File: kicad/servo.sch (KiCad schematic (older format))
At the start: 0 parts

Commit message: Come back to moldova to finish schematics and begin layout
I've started again from Moldova to discuss with Alexander the details.
I'm now working with schematics requeriments.
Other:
- note added: "TEMP"
- note added: "UI"
- note added: "uC\nADC"
- note added: "uC\nCLK\nDbg"
- note added: "uC\nGPIO"
- note removed: "ADC"
- note removed: "CLK\nDBG"
- note removed: "GPIO"
- note removed: "SHUNT\n SD"
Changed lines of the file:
@@
 $Descr A3 16535 11693
 encoding utf-8
-Sheet 1 16
+Sheet 1 17
 Title "servo drive"
 Date "25 10 2019"
@@
 $EndSheet
 $Sheet
-S 7500 7450 1300 1150
+S 5750 7450 1300 1150
 U 5DD0E9D6
-F0 "adc" 50
-F1 "adc.sch" 50
+F0 "uc_adc" 50
+F1 "uc_adc.sch" 50
 $EndSheet
 $Sheet
@@
 $EndSheet
 $Sheet
-S 7500 5900 1300 1150
+S 5750 5900 1300 1150
 U 5EAA846A
-F0 "power" 50
-F1 "power.sch" 50
+F0 "uc_power" 50
+F1 "uc_power.sch" 50
 $EndSheet
 $Sheet
-S 7500 4400 1300 1150
+S 5750 4400 1300 1150
 U 5DD4DF4C
-F0 "clk" 50
-F1 "clk.sch" 50
+F0 "uc_clk_dbg" 50
+F1 "uc_clk_dbg.sch" 50
 $EndSheet
 $Sheet
-S 4100 5900 1300 1150
+S 2350 5900 1300 1150
 U 5DD76B18
 F0 "ac_in" 50
@@
 $EndSheet
 $Sheet
-S 5750 5900 1300 1150
+S 4000 5900 1300 1150
 U 5DF5EE96
 F0 "lem" 50
 F1 "lem.sch" 50
 $EndSheet
-Text Notes 6100 6550 0    197  ~ 39
+Text Notes 4350 6550 0    197  ~ 39
 LEM
-Text Notes 7800 8100 0    197  ~ 39
-ADC
+Text Notes 6050 8300 0    197  ~ 39
+uC\nADC
 $Sheet
-S 5750 7450 1300 1150
+S 4000 7450 1300 1150
 U 5DDE8C5E
 F0 "igbt" 50
 F1 "igbt.sch" 50
 $EndSheet
-Text Notes 6100 8100 0    197  ~ 39
+Text Notes 4350 8100 0    197  ~ 39
 IGBT
-Text Notes 7750 6700 0    197  ~ 39
+Text Notes 5950 6750 0    197  ~ 39
 uC \nPower
 Text Notes 9550 8300 0    197  ~ 39
@@
 S 7500 2900 1300 1150
 U 5DE49152
-F0 "gpio" 50
-F1 "gpio.sch" 50
+F0 "temp" 50
+F1 "temp.sch" 50
 $EndSheet
 Text Notes 7750 3600 0    197  ~ 39
-GPIO
-Text Notes 4550 6700 0    197  ~ 39
+TEMP
+Text Notes 2800 6700 0    197  ~ 39
 AC\nIN
 Text Notes 9500 6700 0    197  ~ 39
 Ether\nNET
-Text Notes 7800 5250 0    197  ~ 39
-CLK\nDBG
+Text Notes 6000 5400 0    197  ~ 39
+uC\nCLK\nDbg
 Text Notes 9500 5050 0    197  ~ 39
 ENDAT
@@
 CAN
 $Sheet
-S 5750 4400 1300 1150
-U 5DEE980E
-F0 "shunt sigma delta" 50
-F1 "shunt_sd.sch" 50
-$EndSheet
-Text Notes 5900 5300 0    197  ~ 39
-SHUNT\n  SD
-$Sheet
-S 5750 2900 1300 1150
+S 4000 2900 1300 1150
 U 5E2F3BE3
 F0 "shunt isolated" 50
 F1 "shunt_iso.sch" 50
 $EndSheet
-Text Notes 5900 3800 0    197  ~ 39
+Text Notes 4150 3800 0    197  ~ 39
 SHUNT\n ISO
+$Sheet
+S 5750 2900 1300 1150
+U 5E033FE4
+F0 "uc_gpio" 50
+F1 "uc_gpio.sch" 50
+$EndSheet
+Text Notes 6050 3750 0    197  ~ 39
+uC\nGPIO
+$Sheet
+S 7500 4400 1300 1150
+U 5E0D58C4
+F0 "ui" 50
+F1 "ui.sch" 50
+$EndSheet
+Text Notes 7950 5100 0    197  ~ 39
+UI
 $EndSCHEMATC

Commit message: added isolated gpi, change digital iso gpo from 2 to 8
I've found some Silabs IC's that match better than texas, are cheaper
and on stock. For digital isolation the GPIO to IGBT and data input from
QRP  and GPI from external switches.
I'm adding these IC's and clean the schematics a lots.
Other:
- note added: "ISO\nGPIO\n"
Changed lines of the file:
@@
 $Descr A3 16535 11693
 encoding utf-8
-Sheet 1 17
+Sheet 1 18
 Title "servo drive"
 Date "25 10 2019"
@@
 S 7500 4400 1300 1150
 U 5E0D58C4
+F0 "isolated gpio" 50
+F1 "iso_gipo.sch" 50
+$EndSheet
+Text Notes 7750 5250 0    197  ~ 39
+ISO\nGPIO\n
+$Sheet
+S 7500 5900 1300 1150
+U 5E72D841
 F0 "ui" 50
 F1 "ui.sch" 50
 $EndSheet
-Text Notes 7950 5100 0    197  ~ 39
+Text Notes 7950 6600 0    197  ~ 39
 UI
 $EndSCHEMATC

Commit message: I've decided LEM lxs series, it's the best..
I've decided to use the LEM lxs, is a new series better than LTS and is
pin to pin compatible with the old one and also CAS series, so I think
it's a good option. 0.5usec rise time, multi prymari turns options, and
so..
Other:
- note added: "SHUNT\nSDELTA"
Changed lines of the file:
@@
 $Descr A3 16535 11693
 encoding utf-8
-Sheet 1 18
+Sheet 1 19
 Title "servo drive"
 Date "25 10 2019"
@@
 F1 "ac_in.sch" 50
 $EndSheet
-$Sheet
-S 4000 5900 1300 1150
-U 5DF5EE96
-F0 "lem" 50
-F1 "lem.sch" 50
-$EndSheet
-Text Notes 4350 6550 0    197  ~ 39
-LEM
 Text Notes 6050 8300 0    197  ~ 39
 uC\nADC
@@
 S 4000 2900 1300 1150
 U 5E2F3BE3
-F0 "shunt isolated" 50
-F1 "shunt_iso.sch" 50
+F0 "shunt isigma delta" 50
+F1 "shunt_sd.sch" 50
 $EndSheet
 Text Notes 4150 3800 0    197  ~ 39
-SHUNT\n ISO
+SHUNT\nSDELTA
 $Sheet
 S 5750 2900 1300 1150
@@
 Text Notes 7950 6600 0    197  ~ 39
 UI
+$Sheet
+S 4000 4450 1300 1150
+U 605B70F2
+F0 "lem" 50
+F1 "lem.sch" 50
+$EndSheet
+Text Notes 4300 5200 0    197  ~ 39
+LEM
+$Sheet
+S 4050 5850 1300 1150
+U 605BEC04
+F0 "shunt isolated" 50
+F1 "shunt_iso.sch" 50
+$EndSheet
+Text Notes 4200 6750 0    197  ~ 39
+SHUNT\n ISO
 $EndSCHEMATC

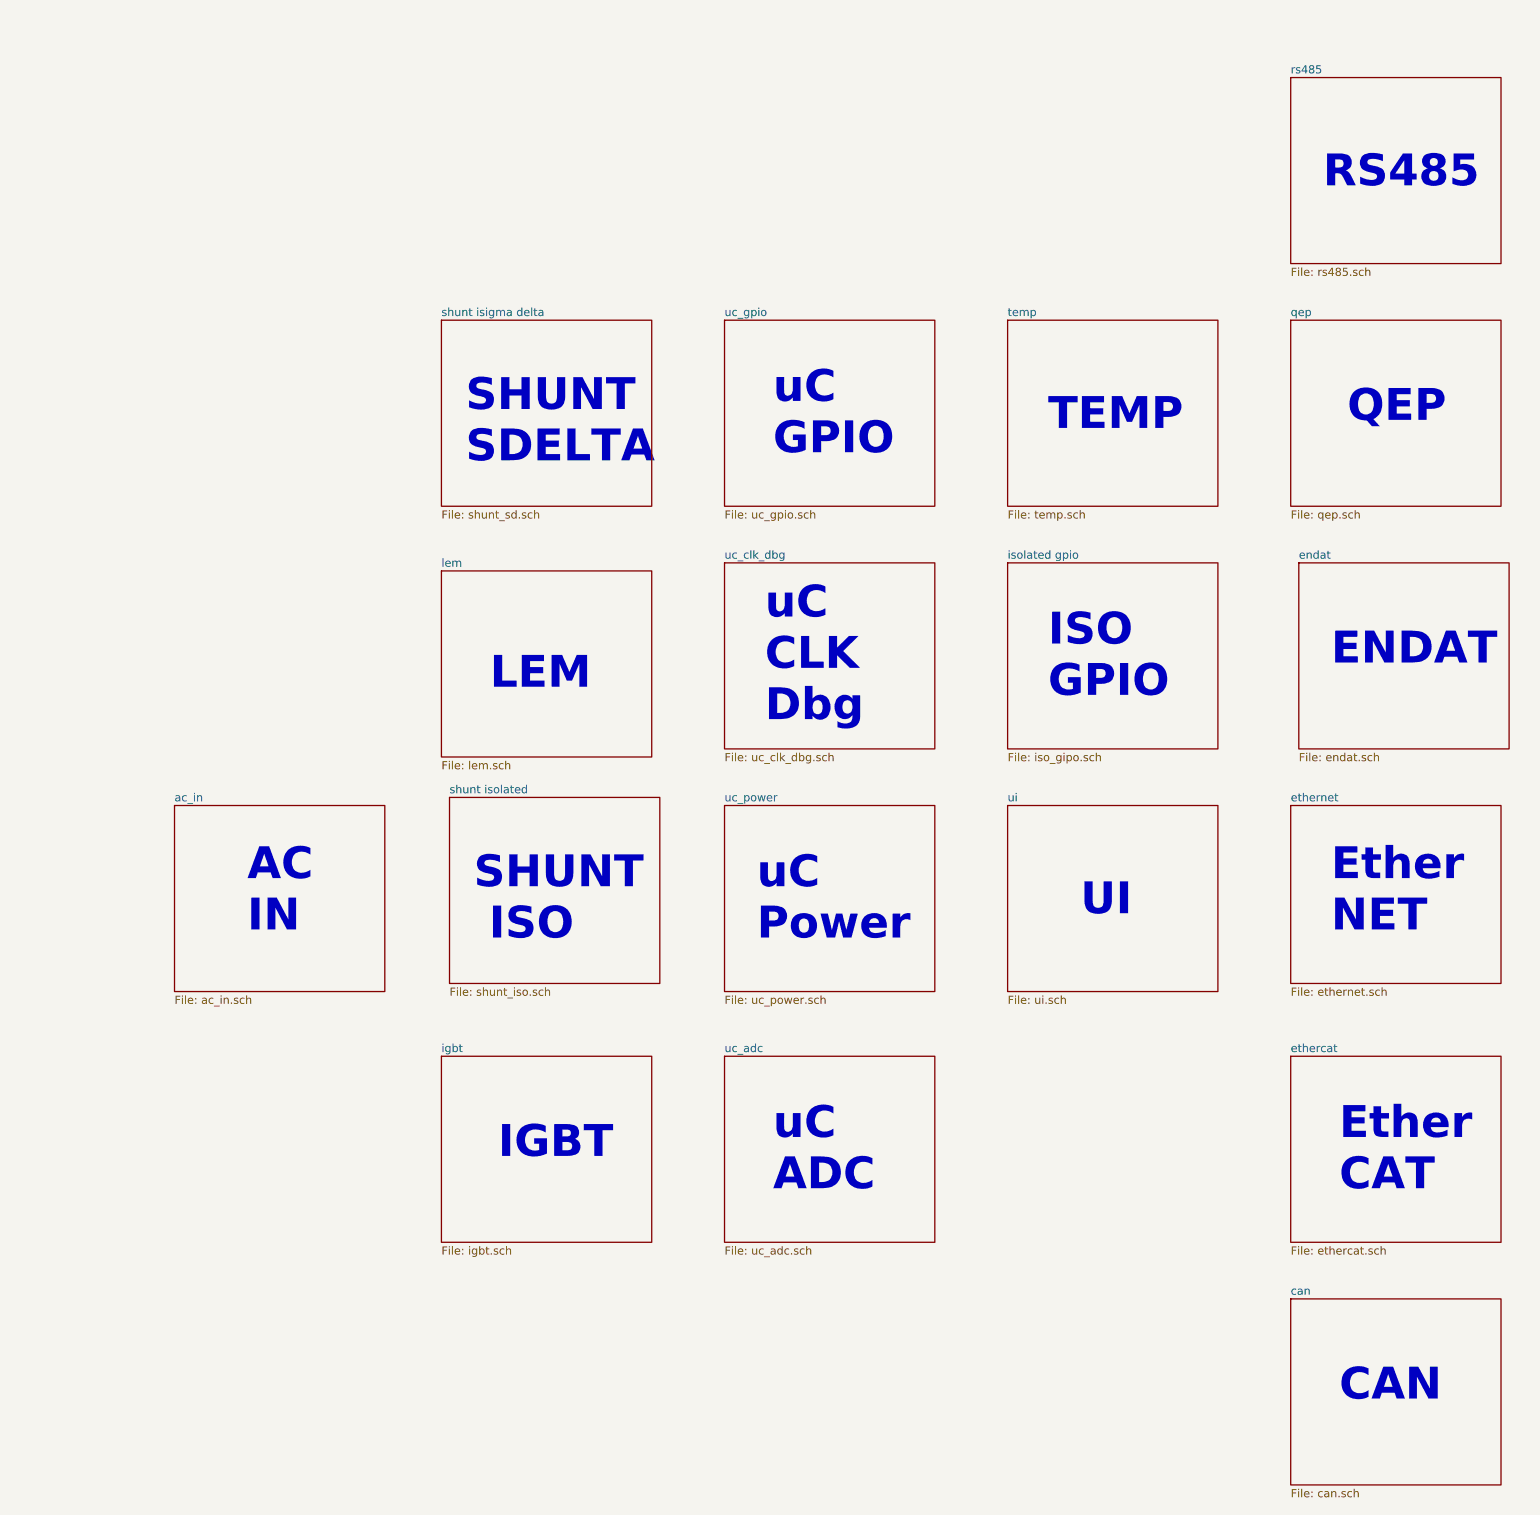
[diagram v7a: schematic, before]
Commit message: I've added LCD UI interfase, EQEP and finish ENDAT
I think I have almos all the interfases ready, I'm begining the
verigication process and then the part definig
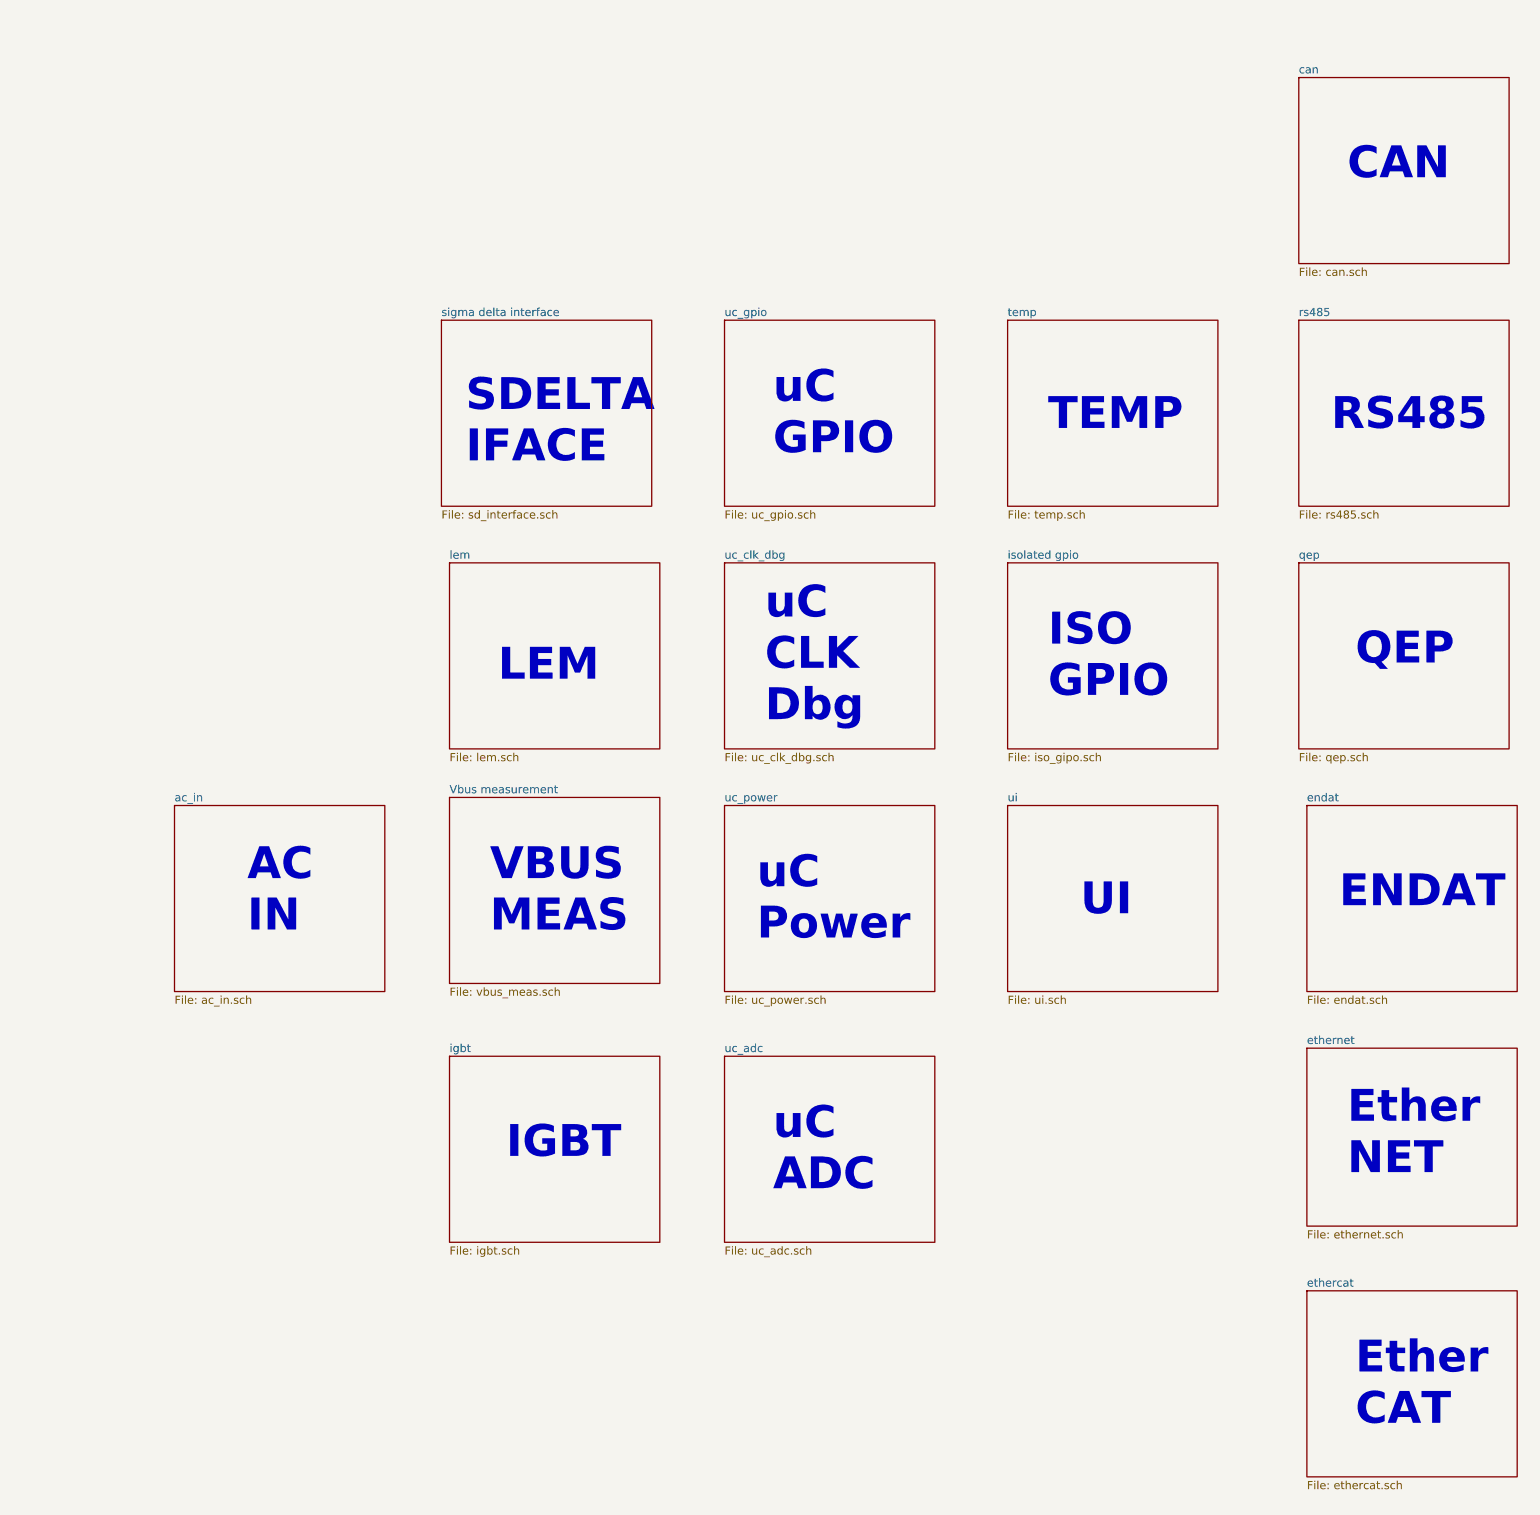
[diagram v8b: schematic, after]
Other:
- note added: "SDELTA\nIFACE"
- note added: "VBUS\nMEAS"
- note removed: "SHUNT\n ISO"
- note removed: "SHUNT\nSDELTA"
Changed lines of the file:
@@
 $EndDescr
 $Sheet
-S 9250 5900 1300 1100
+S 9350 7400 1300 1100
 U 5DC3DC9E
 F0 "ethernet" 50
@@
 $EndSheet
 $Sheet
-S 9250 7450 1300 1150
+S 9350 8900 1300 1150
 U 5DC4A59D
 F0 "ethercat" 50
@@
 uC\nADC
 $Sheet
-S 4000 7450 1300 1150
+S 4050 7450 1300 1150
 U 5DDE8C5E
 F0 "igbt" 50
 F1 "igbt.sch" 50
 $EndSheet
-Text Notes 4350 8100 0    197  ~ 39
+Text Notes 4400 8100 0    197  ~ 39
 IGBT
 Text Notes 5950 6750 0    197  ~ 39
 uC \nPower
-Text Notes 9550 8300 0    197  ~ 39
+Text Notes 9650 9750 0    197  ~ 39
 Ether\nCAT
 $Sheet
@@
 Text Notes 2800 6700 0    197  ~ 39
 AC\nIN
-Text Notes 9500 6700 0    197  ~ 39
+Text Notes 9600 8200 0    197  ~ 39
 Ether\nNET
 Text Notes 6000 5400 0    197  ~ 39
 uC\nCLK\nDbg
-Text Notes 9500 5050 0    197  ~ 39
+Text Notes 9550 6550 0    197  ~ 39
 ENDAT
 $Sheet
-S 9300 4400 1300 1150
+S 9350 5900 1300 1150
 U 5DE3DF56
 F0 "endat" 50
@@
 $EndSheet
 $Sheet
-S 9250 2900 1300 1150
+S 9300 4400 1300 1150
 U 5E092156
 F0 "qep" 50
 F1 "qep.sch" 50
 $EndSheet
-Text Notes 9600 3550 0    197  ~ 39
+Text Notes 9650 5050 0    197  ~ 39
 QEP
 $Sheet
-S 9250 1400 1300 1150
+S 9300 2900 1300 1150
 U 5E1BAEAA
 F0 "rs485" 50
 F1 "rs485.sch" 50
 $EndSheet
-Text Notes 9450 2100 0    197  ~ 39
+Text Notes 9500 3600 0    197  ~ 39
 RS485
 $Sheet
-S 9250 8950 1300 1150
+S 9300 1400 1300 1150
 U 5E21534F
 F0 "can" 50
 F1 "can.sch" 50
 $EndSheet
-Text Notes 9550 9600 0    197  ~ 39
+Text Notes 9600 2050 0    197  ~ 39
 CAN
-$Sheet
-S 4000 2900 1300 1150
-U 5E2F3BE3
-F0 "shunt isigma delta" 50
-F1 "shunt_sd.sch" 50
-$EndSheet
-Text Notes 4150 3800 0    197  ~ 39
-SHUNT\nSDELTA
 $Sheet
 S 5750 2900 1300 1150
@@
 UI
 $Sheet
-S 4000 4450 1300 1150
+S 4050 4400 1300 1150
 U 605B70F2
 F0 "lem" 50
 F1 "lem.sch" 50
 $EndSheet
-Text Notes 4300 5200 0    197  ~ 39
+Text Notes 4350 5150 0    197  ~ 39
 LEM
 $Sheet
 S 4050 5850 1300 1150
 U 605BEC04
-F0 "shunt isolated" 50
-F1 "shunt_iso.sch" 50
+F0 "Vbus measurement" 50
+F1 "vbus_meas.sch" 50
 $EndSheet
-Text Notes 4200 6750 0    197  ~ 39
-SHUNT\n ISO
+Text Notes 4300 6700 0    197  ~ 39
+VBUS\nMEAS
+$Sheet
+S 4000 2900 1300 1150
+U 5EC40F3C
+F0 "sigma delta interface" 50
+F1 "sd_interface.sch" 50
+$EndSheet
+Text Notes 4150 3800 0    197  ~ 39
+SDELTA\nIFACE
 $EndSCHEMATC
